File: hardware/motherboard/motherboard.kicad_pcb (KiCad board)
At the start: 2 copper layers, 175 x 127 mm, 76 parts, among them J1 Conn_01x04_Female, J10 Conn_01x02_Female, J11 Conn_01x02_Female, J12 Conn_01x03_Male, J13 Conn_01x03_Male, J14 Conn_01x03_Male, J15 Conn_01x06_Female, J2 Conn_01x03_Male, J3 Conn_01x05_Female, J4 Conn_01x05_Female, J5 Conn_01x06_Female, J6 Conn_01x05_Female, J7 Conn_01x05_Female, J8 Conn_01x02_Female, J9 Conn_01x03_Female, K2 SANYOU_SRD_Form_C, P1 Conn_02x20_Odd_Even, Q1 BSS138, Q2 BSS138, Q3 BSS138, U1 TDA2003, U2 TDA2003

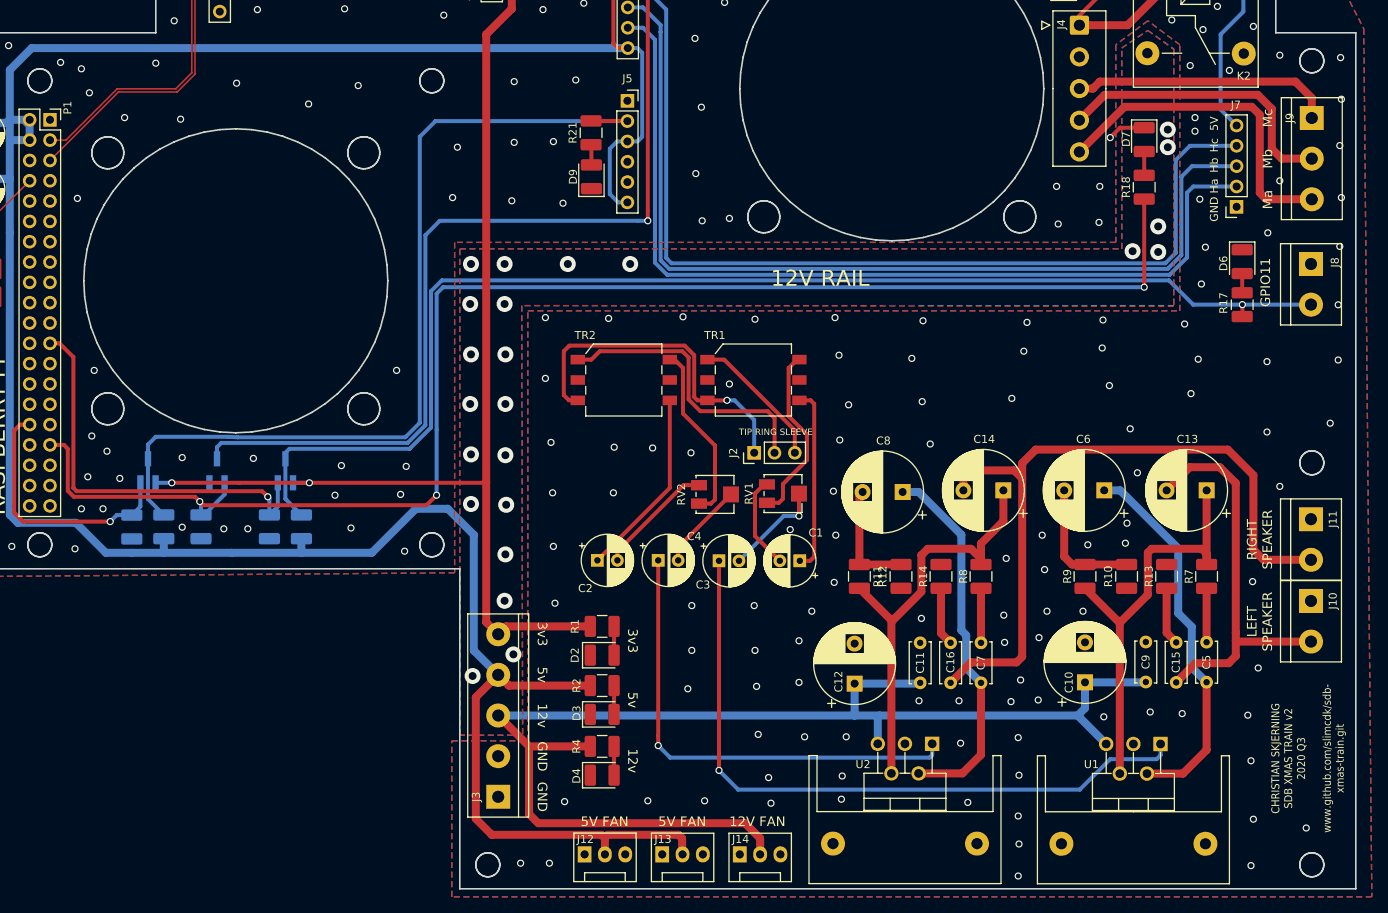
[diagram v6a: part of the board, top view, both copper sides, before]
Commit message: exposed another GPIO
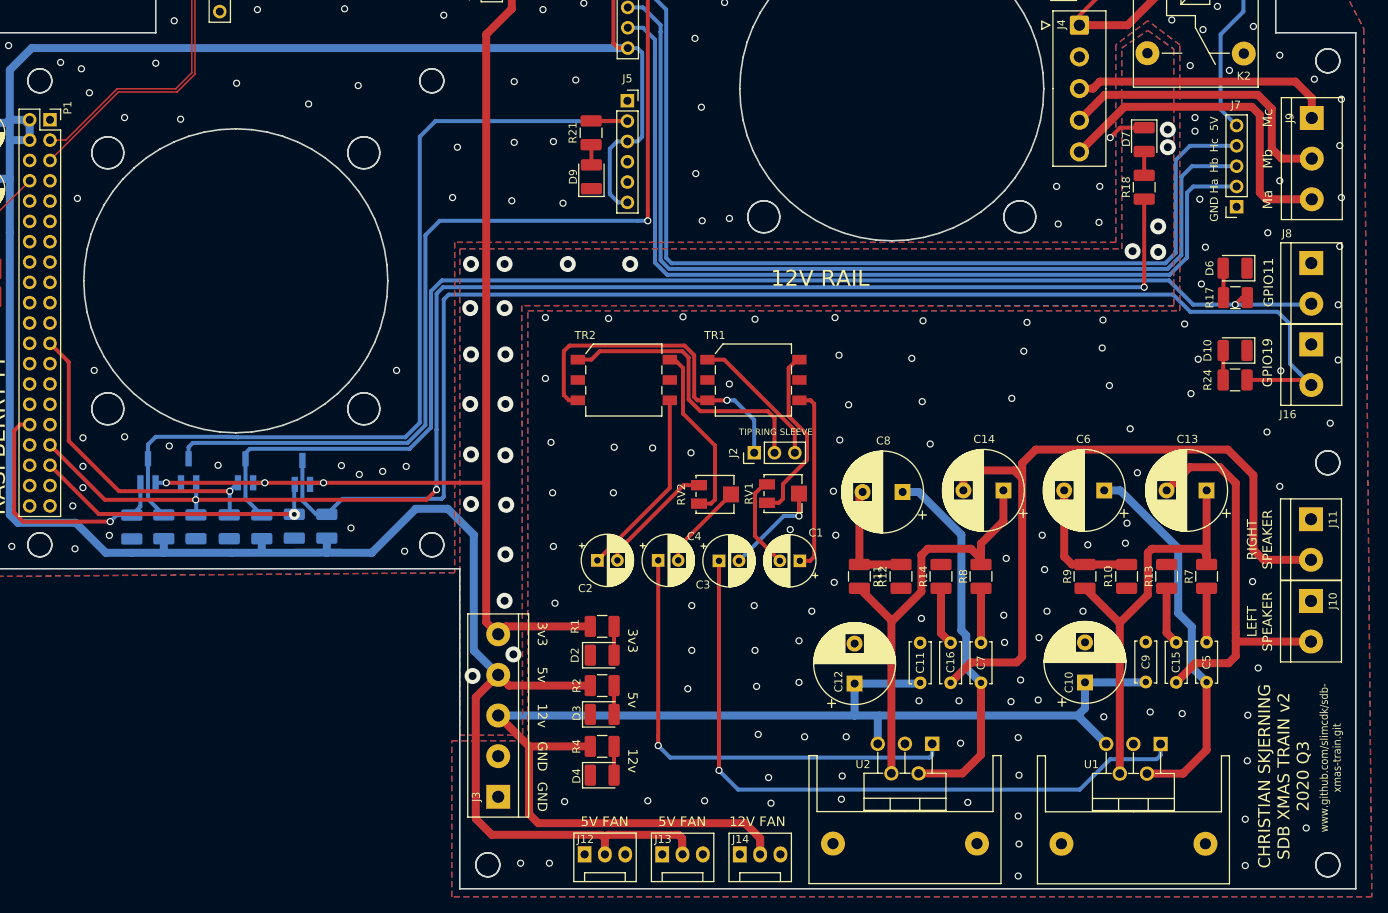
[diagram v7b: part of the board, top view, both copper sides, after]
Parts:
- added D10: LED, LED_SMD:LED_1210_3225Metric_Pad1.42x2.65mm_HandSolder, F.Cu at (184.9, 84.7)
- added J16: Conn_01x02_Female, TerminalBlock:TerminalBlock_bornier-2_P5.08mm, F.Cu at (194.4, 83.9)
- added Q4: BSS138, Package_TO_SOT_SMD:SOT-23_Handsoldering, B.Cu at (68.3, 99.9)
- added R22: 10K, Resistor_SMD:R_1210_3225Metric_Pad1.42x2.65mm_HandSolder, B.Cu at (67.3, 106.7)
- added R23: 10K, Resistor_SMD:R_1210_3225Metric_Pad1.42x2.65mm_HandSolder, B.Cu at (71.4, 106.7)
- added R24: ?, Resistor_SMD:R_1210_3225Metric_Pad1.42x2.65mm_HandSolder, F.Cu at (184.9, 88.4)
- moved R3 5.02 mm to (59.2, 106.8)
- moved Q3 4.99 mm to (61.2, 99.8)
- moved R6 4.95 mm to (63.2, 106.8)
- moved Q2 3.55 mm to (54.1, 99.8)
- moved R17 1.23 mm to (184.9, 78.1), turned to 0 degrees
- moved D6 1.20 mm to (184.9, 74.4), turned to 180 degrees
- moved R15 0.63 mm to (55.0, 106.8)
- moved J8 0.12 mm to (194.4, 73.8)
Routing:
- net Net-(J16-Pad2): track 0.00 -> 173.5 mm
- net /GPIO19(SPI1_MISO): track 0.00 -> 37.1 mm, vias 0 -> 1
- net /GPIO11(SPI0_SCK): track 51.5 -> 40.7 mm
- net /GPIO13(PWM1): track 187.3 -> 180.5 mm
- net Net-(J8-Pad2): track 158.5 -> 163.0 mm
- net Net-(D10-Pad2): track 0.00 -> 3.68 mm
- net Net-(D1-Pad2): track 189.2 -> 192.7 mm
- net +5V: track 447.6 -> 449.4 mm
- net Net-(D6-Pad2): track 2.40 -> 3.70 mm
- net +3V3: track 179.7 -> 180.8 mm, vias 2 -> 3
- net GND: vias 208 -> 205
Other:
- outline, holes or cut-outs redrawn
- board text added: "CHRISTIAN SKJERNING SDB XMAS TRAIN v2 2020 Q3"
- board text added: "GPIO19"
- board text added: "www.github.com/slimcdk/sdb- xmas-train.git"
- board text removed: "CHRISTIAN SKJERNING SDB XMAS TRAIN v2 2020 Q3 www.github.com/slimcdk/sdb- xmas-train.git"

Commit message: gerber files for pcb revision 0.2
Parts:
- moved J3 1.60 mm to (94.4, 140.5)
- moved D5 0.25 mm to (28.5, 78.2)
- moved R5 0.10 mm to (28.5, 74.4)
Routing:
- net +12V: track 158.9 -> 130.4 mm
- net +5V: track 449.4 -> 451.6 mm
- net Net-(C5-Pad2): track 47.6 -> 46.4 mm
- net Net-(C14-Pad1): track 54.0 -> 53.1 mm
- net Net-(C4-Pad1): vias 1 -> 0
- net Net-(C3-Pad1): vias 1 -> 0
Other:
- board text added: "SLEEVE RING TIP"
- board text added: "github.com/slimcdk/ sdb-xmas-train"
- board text removed: "TIP RING SLEEVE"
- board text removed: "www.github.com/slimcdk/sdb- xmas-train.git"
